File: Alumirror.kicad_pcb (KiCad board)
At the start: 2 copper layers, 139.7 x 88.9 mm, 96 parts, among them J1 USB_C_Receptacle_USB2.0_16P_2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, J2 USB_C_Receptacle_USB2.0_16P_2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, J3 USB_C_Receptacle_USB2.0_16P_2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, J4 USB_C_Receptacle_USB2.0_16P_2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, K11 PG1350, K12 PG1350, K13 PG1350, K14 PG1350, K15 PG1350, K16 PG1350, K21 PG1350, K22 PG1350, K23 PG1350, K24 PG1350, K25 PG1350, K26 PG1350, K31 PG1350, K32 PG1350, K33 PG1350, K34 PG1350, K35 PG1350, K36 PG1350_1½U, K41 PG1350_1½U, K42 PG1350/SKQUCAA010, SW10 BOOT, U1 CH552T, U2 CH552T, U3 USBLC6-2P6, U4 USBLC6-2P6, U5 USBLC6-2P6, U6 USBLC6-2P6

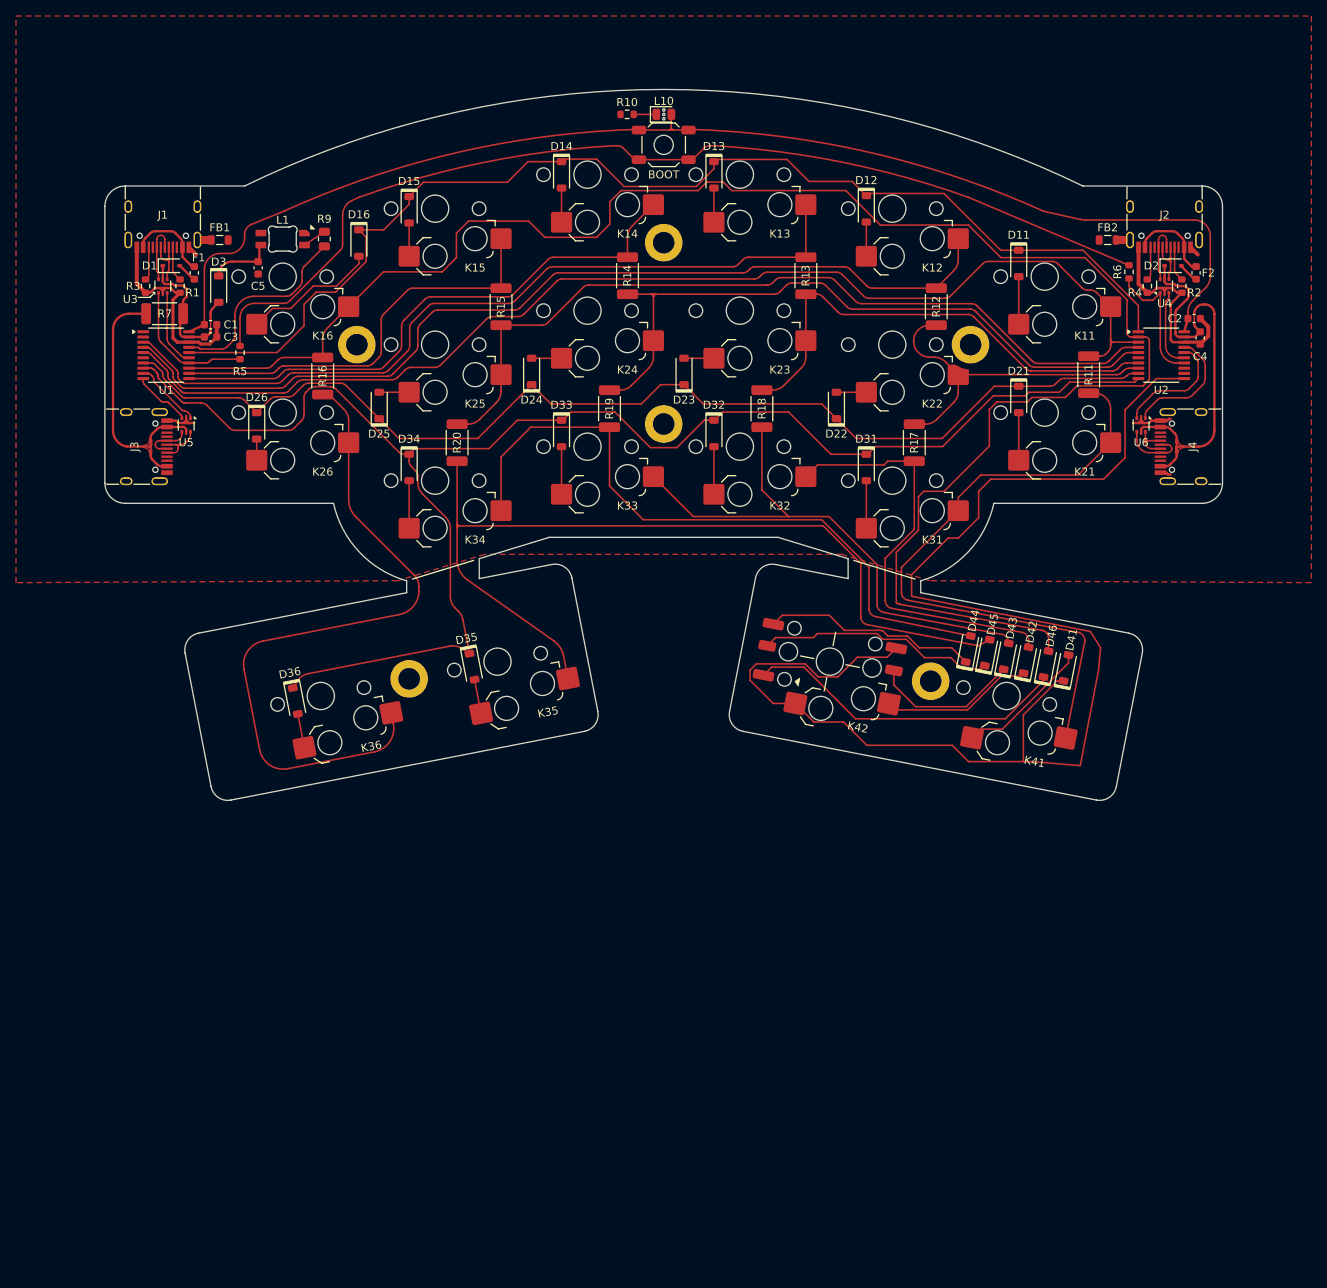
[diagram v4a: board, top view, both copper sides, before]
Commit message: Test left-hand only components, outline and routing
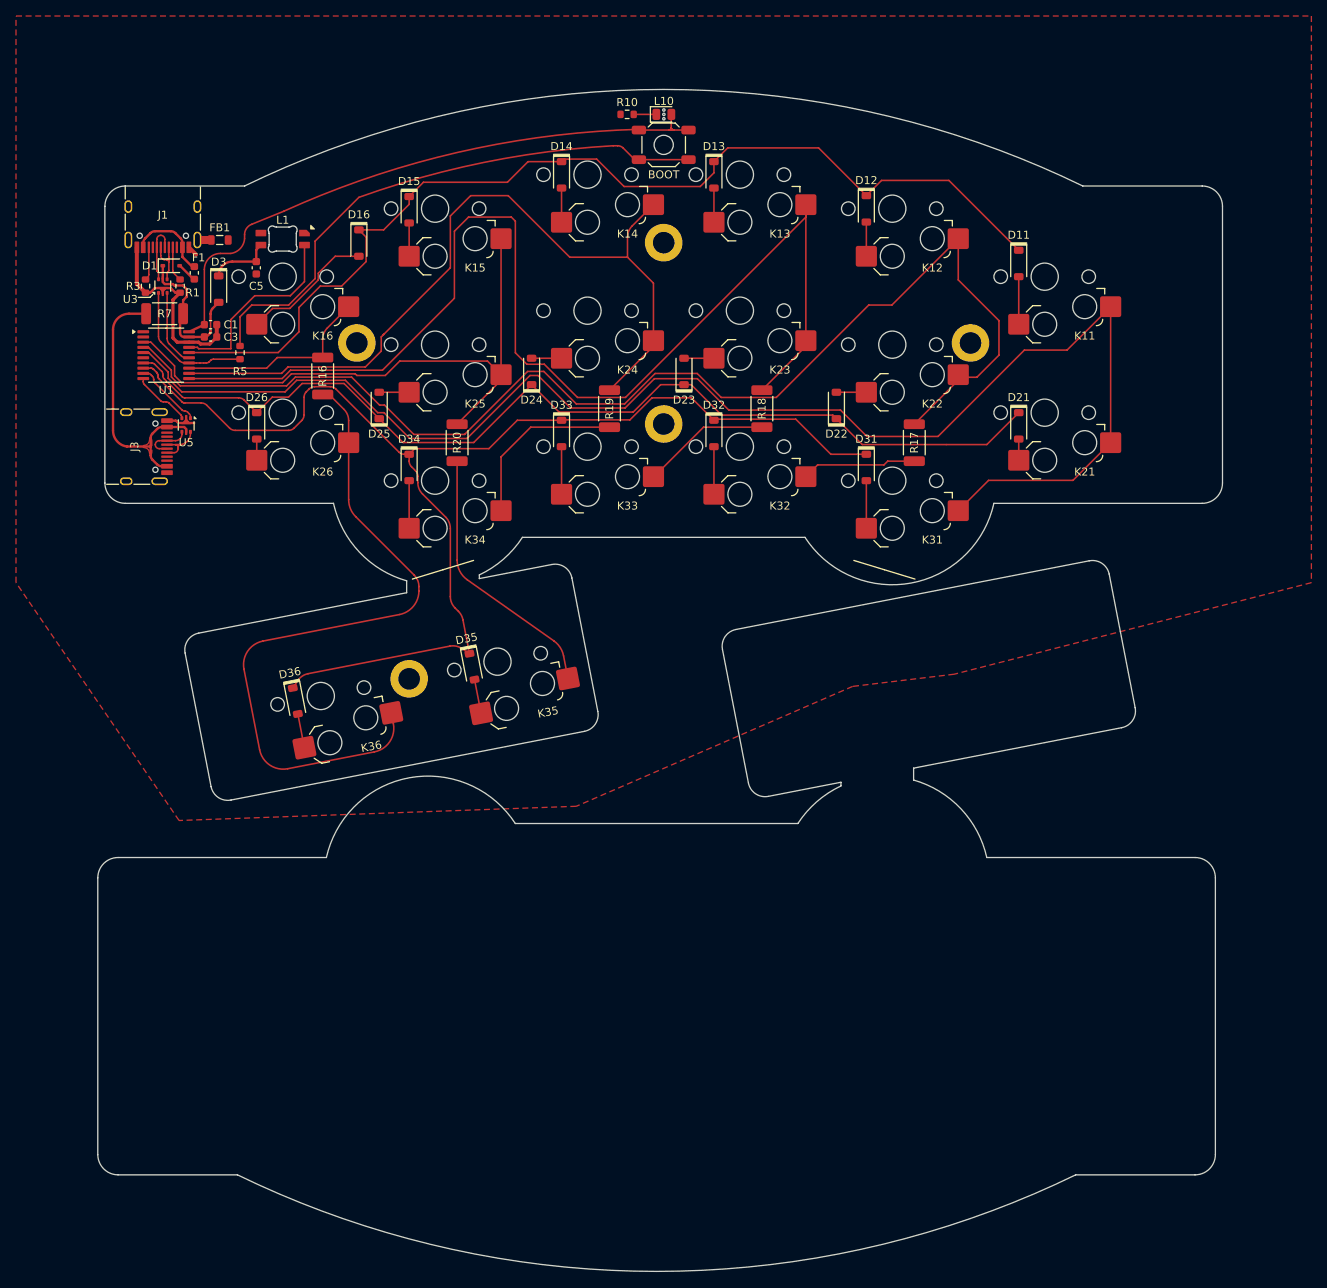
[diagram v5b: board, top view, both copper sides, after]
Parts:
- removed C2, C4: 100nF, Capacitor_SMD:C_0603_1608Metric
- removed D2: PMEG2010EA, Diode_SMD:D_SOD-323
- removed D41, D42, D43, D44, D45, D46: 1N4148, Project Library:D_SOD-123
- removed F2: 500mA, Fuse:Fuse_0603_1608Metric
- removed FB2: FerriteBead, Inductor_SMD:L_0805_2012Metric
- removed H6: MountingHole, Project Library:MountingHole_2.2mm_M2_SMD_Solder_Nut
- removed J2, J4: USB_C_Receptacle_USB2.0_16P_2SH, Project Library:USB_C_Receptacle_HRO_TYPE-C-31-M-12
- removed K41: PG1350_1½U, Project Library:SW_choc_v1_HS_CPG135001S30_1layer_1.5u
- removed K42: PG1350/SKQUCAA010, Project Library:SW_choc_v1_HS_nav_CPG135001S30_SKQUCAA010_1layer_1u_1
- removed NT2: NetTie_2, Project Library:NetTie-2_SMD_Pad0.2mm
- removed R11, R12, R13, R14, R15: 0R, Project Library:R_2010_5025Metric_Mod
- removed R2, R4: 5k1, Resistor_SMD:R_0603_1608Metric
- removed R6: 5k1-20k, Resistor_SMD:R_0603_1608Metric
- removed R9: 470R, Resistor_SMD:R_0805_2012Metric
- removed U2: CH552T, Package_SO:TSSOP-20_4.4x6.5mm_P0.65mm
- removed U4, U6: USBLC6-2P6, Project Library:SOT-666_Mod
- K22: footprint Project Library:SW_choc_v1_HS_CPG135001S30_1layer_1u_clipped -> Project Library:SW_choc_v1_HS_CPG135001S30_1layer_1u
- moved D21 3.30 mm to (196.8, 71.1)
- moved C5 0.23 mm to (101.5, 51.3)
- moved H1 0.21 mm to (114.0, 60.7)
- moved H4 0.21 mm to (190.8, 60.7)
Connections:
- net Col2RT renamed Net-(K32-Pad1)
- net Col3RT renamed Net-(K33-Pad1)
- net Col4RT renamed Net-(K34-Pad1)
- K12 pad 1: Col2L -> Col2
- K13 pad 1: Col3L -> Col3
- K14 pad 1: Col4L -> Col4
- K15 pad 1: Col5L -> Col5
- K21 pad 1: Col1T -> Col1
- K22 pad 1: Col2R -> Col2
- K23 pad 1: Col3R -> Col3
- K24 pad 1: Col4R -> Col4
- K25 pad 1: Col5R -> Col5
- K31 pad 1: Col1T -> Col1
- L1 pad 3: Net-(L1-DIN) -> LED
- R17 pad 1: Col2R -> Col2
- R18 pad 1: Col3R -> Col3
- R19 pad 1: Col4R -> Col4
- R20 pad 1: Col5R -> Col5
- U1 pad 11: Col4L -> Col3
- U1 pad 12: Col5L -> Col4
- U1 pad 3: Col3L -> Col5
- U1 pad 4: Col2L -> Col2
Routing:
- net Col6: track 225.6 -> 24.9 mm
- net Row4R: track 172.6 -> 0.00 mm
- net Col2: track 0.00 -> 153.9 mm
- net Col3: track 0.00 -> 145.0 mm
- net Col2L: track 117.4 -> 0.00 mm
- net Col5R: track 102.7 -> 0.00 mm
- net Col3L: track 99.8 -> 0.00 mm
- net Col4: track 0.00 -> 99.7 mm
- net Col4R: track 84.5 -> 0.00 mm
- net Col1T: track 80.8 -> 0.00 mm
- net Col5T: track 109.8 -> 33.6 mm
- net Col5: track 0.00 -> 74.3 mm
- net Col4L: track 70.5 -> 0.00 mm
- net Net-(K34-Pad1): track 84.5 -> 21.8 mm
- net Col3R: track 61.0 -> 0.00 mm
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- removed copper zone on F.Cu, net VCC_R
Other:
- board size 139.7 x 88.9 mm -> 140.6 x 147.7 mm

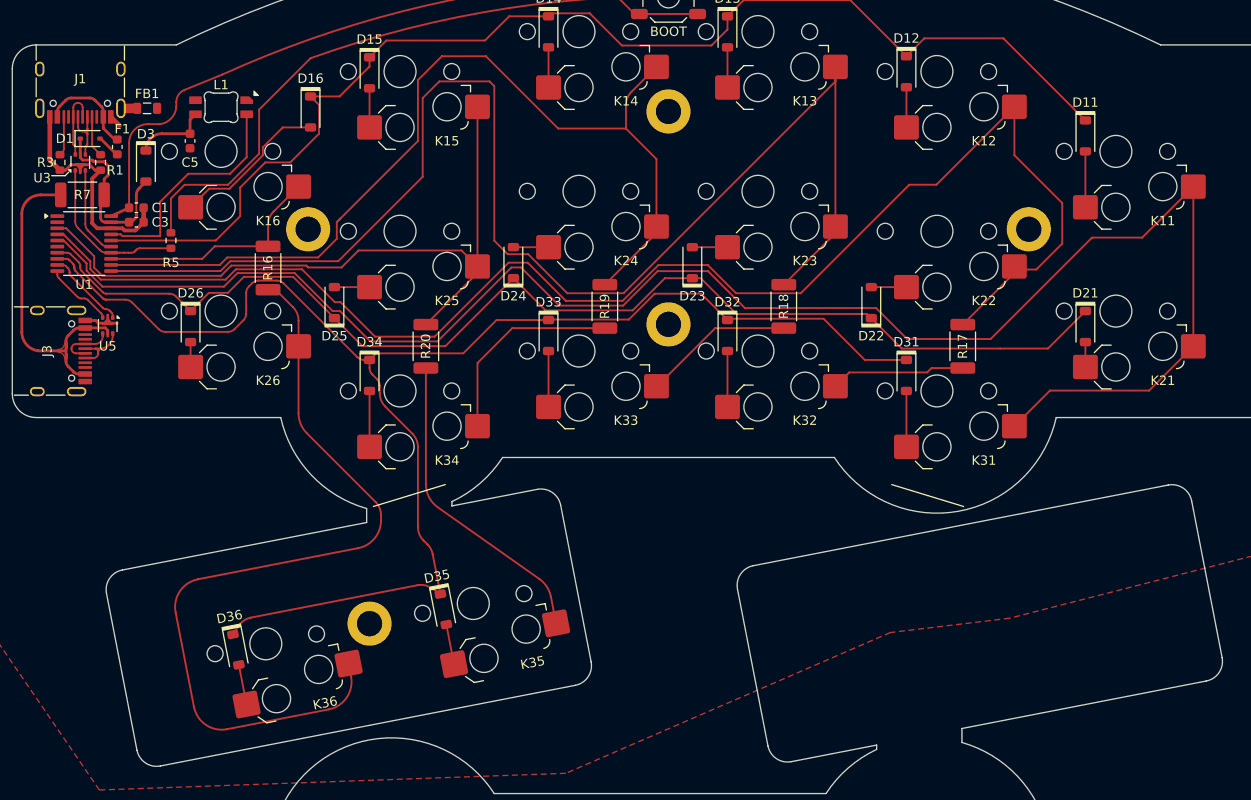
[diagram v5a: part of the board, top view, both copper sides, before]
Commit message: Change thumb keys to columns 1 and 6
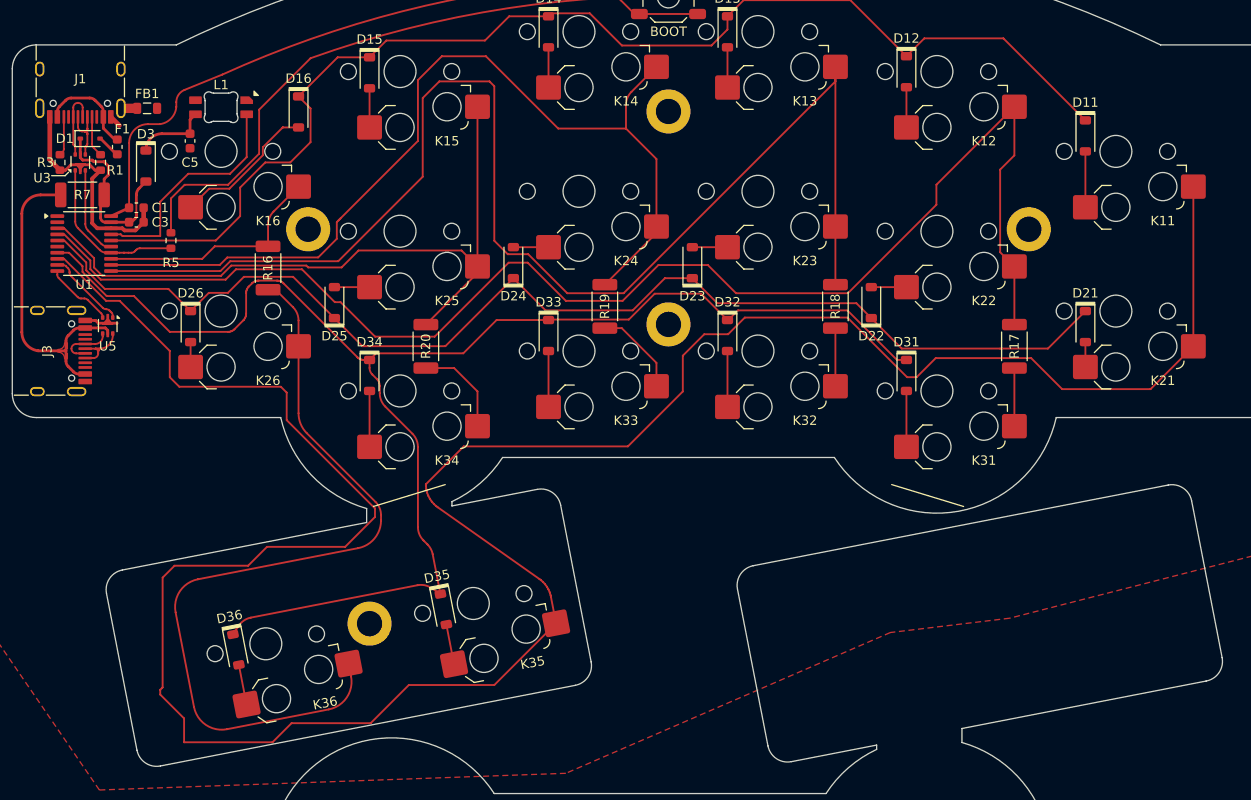
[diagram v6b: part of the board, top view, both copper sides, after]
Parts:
- moved R17 5.50 mm to (189.2, 73.2)
- moved R18 5.49 mm to (170.2, 68.9)
- moved D16 1.28 mm to (113.0, 48.2)
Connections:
- K31 pad 1: Col1 -> Net-(K31-Pad1)
- K35 pad 1: Col5T -> Col1
- R17 pad 2: Net-(K32-Pad1) -> Net-(K31-Pad1)
- R18 pad 2: Net-(K33-Pad1) -> Net-(K32-Pad1)
- R19 pad 2: Net-(K34-Pad1) -> Net-(K33-Pad1)
- R20 pad 2: Col5T -> Net-(K34-Pad1)
- U1 pad 5: Col1 -> Row2
- U1 pad 7: Row2 -> Row3
- U1 pad 8: Row3 -> Col1
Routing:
- net Col1: track 182.2 -> 274.2 mm
- net Col5T: track 33.6 -> 0.00 mm
- net Net-(K34-Pad1): track 21.8 -> 10.2 mm
- net Net-(K32-Pad1): track 14.4 -> 6.19 mm
- net Net-(K33-Pad1): track 16.0 -> 9.52 mm
- net Net-(K31-Pad1): track 0.00 -> 6.19 mm
- net Col2: track 153.9 -> 149.5 mm
- net Col3: track 145.0 -> 143.4 mm
- net Row3: track 157.2 -> 158.5 mm
- net Net-(D16-A): track 16.8 -> 15.5 mm
- net Row2: track 127.4 -> 128.2 mm

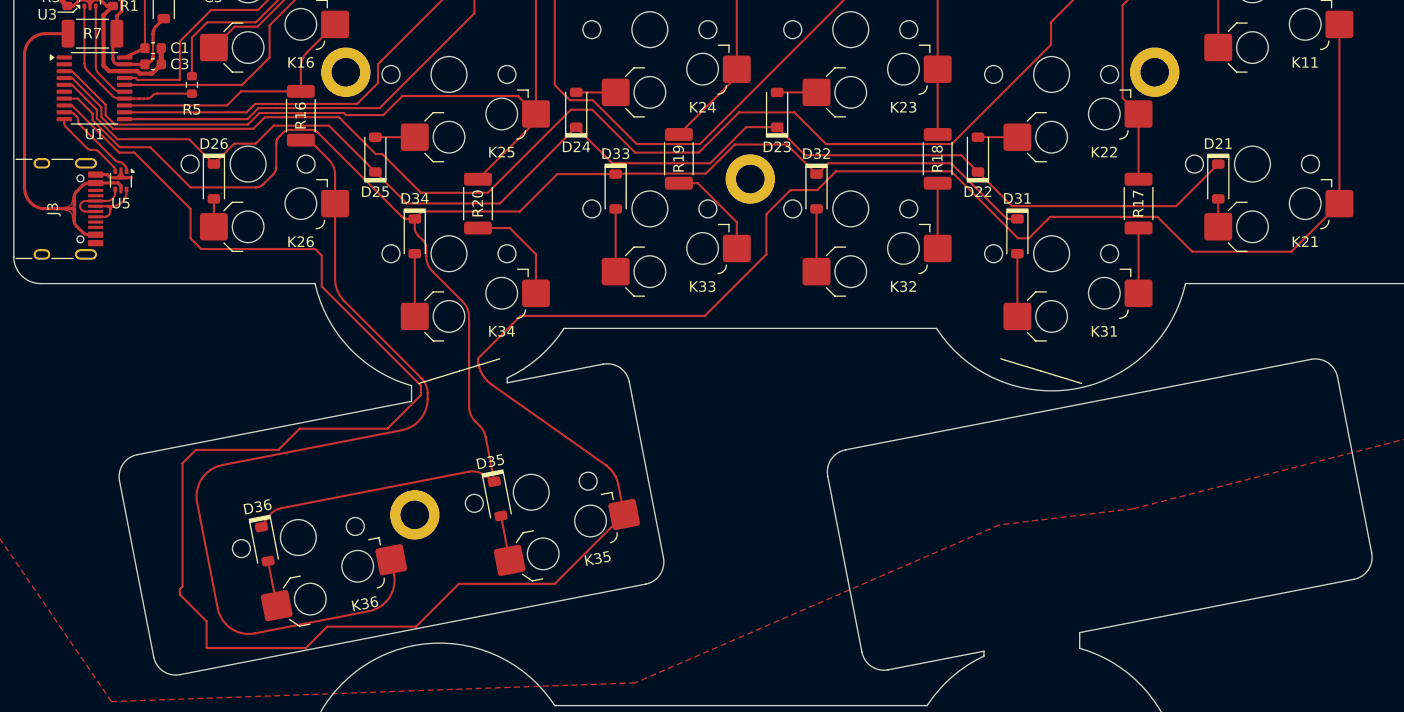
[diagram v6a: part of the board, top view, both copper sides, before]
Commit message: Move thumb keys to new Row 4
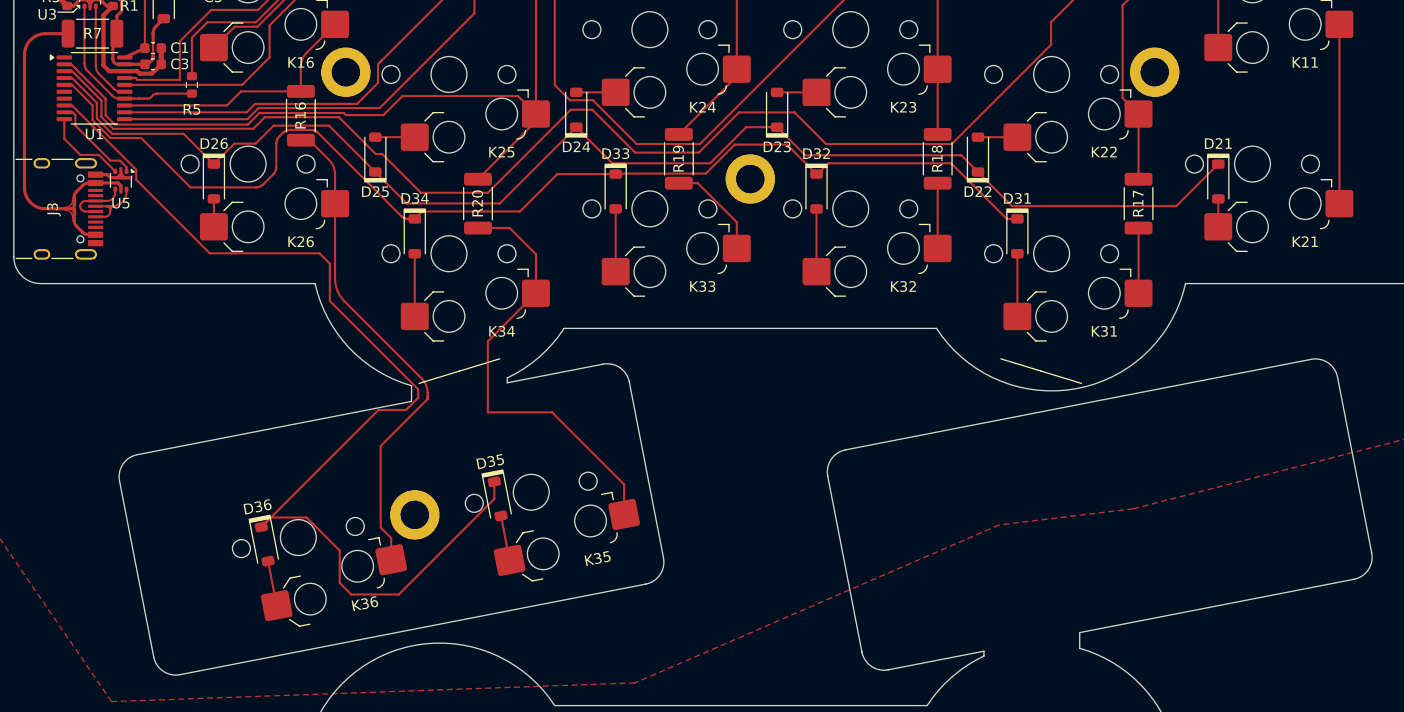
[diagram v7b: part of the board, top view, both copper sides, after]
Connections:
- D35 pad 1: Row3 -> Row4
- D36 pad 1: Row3 -> Row4
- K34 pad 1: Net-(K34-Pad1) -> Col5T
- K35 pad 1: Col1 -> Col5T
- R20 pad 2: Net-(K34-Pad1) -> Col5T
- U1 pad 2: unconnected-(U1-P1.4-Pad2) -> Col5
- U1 pad 3: Col5 -> Col2
- U1 pad 4: Col2 -> Row2
- U1 pad 5: Row2 -> Row3
- U1 pad 7: Row3 -> Col1
- U1 pad 8: Col1 -> Row4
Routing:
- net Col1: track 274.2 -> 17.0 mm
- net Row4: track 0.00 -> 100.8 mm
- net Row3: track 158.5 -> 108.7 mm
- net Col5T: track 0.00 -> 42.0 mm
- net Col6T: track 86.8 -> 46.6 mm
- net Net-(K34-Pad1): track 10.2 -> 0.00 mm
- net TX_L: track 8.03 -> 9.04 mm
- net RX_L: track 7.22 -> 7.98 mm
- net Row2: track 128.2 -> 128.8 mm
- net Col2: track 149.5 -> 150.2 mm
- net Col5: track 74.2 -> 74.8 mm

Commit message: Various tweaks
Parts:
- removed R17: 0R, Project Library:R_2010_5025Metric_Mod
- removed R7: 0R, Resistor_SMD:R_2010_5025Metric
- moved NT1 1.31 mm to (94.4, 61.9)
- moved U1 1.31 mm to (90.2, 60.9)
- moved C1 1.28 mm to (95.8, 57.1)
- moved C3 1.28 mm to (95.8, 58.7)
- moved R5 0.84 mm to (99.4, 61.1)
- moved H1 0.25 mm to (114.3, 60.7)
- moved H4 0.25 mm to (190.5, 60.7)
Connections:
- J3 pad A4: VCC_L' -> VCC_L
- J3 pad A9: VCC_L' -> VCC_L
- J3 pad B4: VCC_L' -> VCC_L
- J3 pad B9: VCC_L' -> VCC_L
- K31 pad 1: Net-(K31-Pad1) -> Col2
- U1 pad 11: Col3 -> Col5
- U1 pad 2: Col5 -> Col3
- U1 pad 4: Row2 -> Col1
- U1 pad 5: Row3 -> Row2
- U1 pad 7: Col1 -> Row3
- U5 pad 5: VCC_L' -> VCC_L
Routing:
- net Col1: track 17.0 -> 183.2 mm
- net VCC_L: track 18.6 -> 55.7 mm
- net VCC_L': track 34.1 -> 0.00 mm
- net Row2: track 128.8 -> 150.0 mm
- net Col3: track 143.4 -> 129.2 mm
- net Col2: track 150.2 -> 162.0 mm
- net Col5: track 74.8 -> 65.0 mm
- net Net-(K31-Pad1): track 6.19 -> 0.00 mm
- net GND: track 25.8 -> 20.9 mm
- net Row4: track 100.8 -> 102.3 mm
- net LED: track 24.7 -> 23.4 mm
- net +3V3: track 29.9 -> 28.7 mm
- net USB_L-: track 9.26 -> 8.36 mm
- net BOOT: track 37.0 -> 36.2 mm
- net TX_L: track 9.04 -> 9.79 mm
- added copper zone on F.Cu, net Col4
- added copper zone on F.Cu, net VCC_L
- removed copper zone on F.Cu, net VCC_L'
